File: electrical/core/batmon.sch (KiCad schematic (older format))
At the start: 25 parts

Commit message: Supply and Enable
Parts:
- gave numbers to parts that had none: 25
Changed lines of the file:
@@
 $Descr A4 11693 8268
 encoding utf-8
-Sheet 7 7
+Sheet 7 8
 Title ""
 Date ""
@@
 $EndDescr
 $Comp
-L rasbot:BQ76925 U?
+L rasbot:BQ76925 U5
 U 1 1 5D9FCD19
 P 5750 3650
-F 0 "U?" H 5750 4531 50  0000 C CNN
+F 0 "U5" H 5750 4531 50  0000 C CNN
 F 1 "BQ76925" H 5750 4440 50  0000 C CNN
 F 2 "Package_SO:TSSOP-20_4.4x6.5mm_P0.65mm" H 5650 3950 50  0001 C CNN
@@
 $EndComp
 $Comp
-L Device:R RIN?
+L Device:R RIN1
 U 1 1 5D9FCD1F
 P 3400 2700
-F 0 "RIN?" V 3193 2700 50  0000 C CNN
+F 0 "RIN1" V 3193 2700 50  0000 C CNN
 F 1 "47" V 3284 2700 50  0000 C CNN
 F 2 "Resistor_SMD:R_0805_2012Metric" V 3330 2700 50  0001 C CNN
@@
 $EndComp
 $Comp
-L Device:R RIN?
+L Device:R RIN2
 U 1 1 5D9FCD25
 P 3400 3200
-F 0 "RIN?" V 3193 3200 50  0000 C CNN
+F 0 "RIN2" V 3193 3200 50  0000 C CNN
 F 1 "47" V 3284 3200 50  0000 C CNN
 F 2 "Resistor_SMD:R_0805_2012Metric" V 3330 3200 50  0001 C CNN
@@
 $EndComp
 $Comp
-L Device:C CIN?
+L Device:C CIN2
 U 1 1 5D9FCD2B
 P 3800 3450
-F 0 "CIN?" H 3915 3496 50  0000 L CNN
+F 0 "CIN2" H 3915 3496 50  0000 L CNN
 F 1 "1u" H 3915 3405 50  0000 L CNN
 F 2 "Capacitor_SMD:C_0805_2012Metric" H 3838 3300 50  0001 C CNN
@@
 $EndComp
 $Comp
-L Device:R RIN?
+L Device:R RIN3
 U 1 1 5D9FCD31
 P 3400 3700
-F 0 "RIN?" V 3193 3700 50  0000 C CNN
+F 0 "RIN3" V 3193 3700 50  0000 C CNN
 F 1 "47" V 3284 3700 50  0000 C CNN
 F 2 "Resistor_SMD:R_0805_2012Metric" V 3330 3700 50  0001 C CNN
@@
 $EndComp
 $Comp
-L Device:C CIN?
+L Device:C CIN3
 U 1 1 5D9FCD37
 P 3800 3950
-F 0 "CIN?" H 3915 3996 50  0000 L CNN
+F 0 "CIN3" H 3915 3996 50  0000 L CNN
 F 1 "1u" H 3915 3905 50  0000 L CNN
 F 2 "Capacitor_SMD:C_0805_2012Metric" H 3838 3800 50  0001 C CNN
@@
 $EndComp
 $Comp
-L Device:R RIN?
+L Device:R RIN4
 U 1 1 5D9FCD3D
 P 3400 4200
-F 0 "RIN?" V 3193 4200 50  0000 C CNN
+F 0 "RIN4" V 3193 4200 50  0000 C CNN
 F 1 "47" V 3284 4200 50  0000 C CNN
 F 2 "Resistor_SMD:R_0805_2012Metric" V 3330 4200 50  0001 C CNN
@@
 $EndComp
 $Comp
-L Device:C CIN?
+L Device:C CIN1
 U 1 1 5D9FCD43
 P 3800 2950
-F 0 "CIN?" H 3915 2996 50  0000 L CNN
+F 0 "CIN1" H 3915 2996 50  0000 L CNN
 F 1 "1u" H 3915 2905 50  0000 L CNN
 F 2 "Capacitor_SMD:C_0805_2012Metric" H 3838 2800 50  0001 C CNN
@@
 	3550 4200 3800 4200
 $Comp
-L Connector:Conn_01x04_Male J?
+L Connector:Conn_01x04_Male J13
 U 1 1 5D9FCD55
 P 2050 3500
-F 0 "J?" H 1800 3300 50  0000 L CNN
+F 0 "J13" H 1800 3300 50  0000 L CNN
 F 1 "Conn_01x04" H 1800 3200 50  0000 L CNN
 F 2 "Connector_PinHeader_2.54mm:PinHeader_1x04_P2.54mm_Vertical" H 2050 3500 50  0001 C CNN
@@
 $EndComp
 $Comp
-L Device:C CIN?
+L Device:C CIN4
 U 1 1 5D9FCD5B
 P 3800 4450
-F 0 "CIN?" H 3915 4496 50  0000 L CNN
+F 0 "CIN4" H 3915 4496 50  0000 L CNN
 F 1 "1u" H 3915 4405 50  0000 L CNN
 F 2 "Capacitor_SMD:C_0805_2012Metric" H 3838 4300 50  0001 C CNN
@@
 	5750 4600 5750 4350
 $Comp
-L power:GND #PWR?
+L power:GND #PWR044
 U 1 1 5D9FCD71
 P 4600 4600
-F 0 "#PWR?" H 4600 4350 50  0001 C CNN
+F 0 "#PWR044" H 4600 4350 50  0001 C CNN
 F 1 "GND" H 4605 4427 50  0000 C CNN
 F 2 "" H 4600 4600 50  0001 C CNN
@@
 	4300 3700 3800 3700
 $Comp
-L power:GND #PWR?
+L power:GND #PWR045
 U 1 1 5D9FCD81
 P 4900 2450
-F 0 "#PWR?" H 4900 2200 50  0001 C CNN
+F 0 "#PWR045" H 4900 2200 50  0001 C CNN
 F 1 "GND" H 4905 2277 50  0000 C CNN
 F 2 "" H 4900 2450 50  0001 C CNN
@@
 	4650 2000 4900 2000
 $Comp
-L Device:C CBAT?
+L Device:C CBAT1
 U 1 1 5D9FCD8A
 P 4900 2200
-F 0 "CBAT?" H 5015 2246 50  0000 L CNN
+F 0 "CBAT1" H 5015 2246 50  0000 L CNN
 F 1 "10u" H 5015 2155 50  0000 L CNN
 F 2 "Capacitor_SMD:C_0805_2012Metric" H 4938 2050 50  0001 C CNN
@@
 $EndComp
 $Comp
-L Device:C COUT?
+L Device:C COUT2
 U 1 1 5D9FCD90
 P 5450 5050
-F 0 "COUT?" H 5565 5096 50  0000 L CNN
+F 0 "COUT2" H 5565 5096 50  0000 L CNN
 F 1 "1u" H 5565 5005 50  0000 L CNN
 F 2 "Capacitor_SMD:C_0805_2012Metric" H 5488 4900 50  0001 C CNN
@@
 $EndComp
 $Comp
-L Device:C COUT?
+L Device:C COUT1
 U 1 1 5D9FCD96
 P 4550 5050
-F 0 "COUT?" H 4665 5096 50  0000 L CNN
+F 0 "COUT1" H 4665 5096 50  0000 L CNN
 F 1 "1u" H 4665 5005 50  0000 L CNN
 F 2 "Capacitor_SMD:C_0805_2012Metric" H 4588 4900 50  0001 C CNN
@@
 Connection ~ 4550 4900
 $Comp
-L Device:C CREF?
+L Device:C CREF1
 U 1 1 5D9FCDA7
 P 8750 2850
-F 0 "CREF?" H 8865 2896 50  0000 L CNN
+F 0 "CREF1" H 8865 2896 50  0000 L CNN
 F 1 "10u" H 8865 2805 50  0000 L CNN
 F 2 "Capacitor_SMD:C_0805_2012Metric" H 8788 2700 50  0001 C CNN
@@
 $EndComp
 $Comp
-L power:GND #PWR?
+L power:GND #PWR048
 U 1 1 5D9FCDAD
 P 8000 3500
-F 0 "#PWR?" H 8000 3250 50  0001 C CNN
+F 0 "#PWR048" H 8000 3250 50  0001 C CNN
 F 1 "GND" H 8005 3327 50  0000 C CNN
 F 2 "" H 8000 3500 50  0001 C CNN
@@
 $EndComp
 $Comp
-L power:GND #PWR?
+L power:GND #PWR046
 U 1 1 5D9FCDB3
 P 5000 5350
-F 0 "#PWR?" H 5000 5100 50  0001 C CNN
+F 0 "#PWR046" H 5000 5100 50  0001 C CNN
 F 1 "GND" H 5005 5177 50  0000 C CNN
 F 2 "" H 5000 5350 50  0001 C CNN
@@
 Battery_OvercurrentAlert
 $Comp
-L Device:C CSENSE?
+L Device:C CSENSE1
 U 1 1 5D9FCDC2
 P 7850 4850
-F 0 "CSENSE?" V 8100 4800 50  0000 L CNN
+F 0 "CSENSE1" V 8100 4800 50  0000 L CNN
 F 1 "0.1u" V 8000 4800 50  0000 L CNN
 F 2 "Capacitor_SMD:C_0805_2012Metric" H 7888 4700 50  0001 C CNN
@@
 $EndComp
 $Comp
-L Device:R RSENSEN?
+L Device:R RSENSEN1
 U 1 1 5D9FCDC8
 P 7250 5200
-F 0 "RSENSEN?" H 7000 5300 50  0000 C CNN
+F 0 "RSENSEN1" H 7000 5300 50  0000 C CNN
 F 1 "1k" H 7134 5200 50  0000 C CNN
 F 2 "Resistor_SMD:R_0805_2012Metric" V 7180 5200 50  0001 C CNN
@@
 $EndComp
 $Comp
-L Device:R RSENSEP?
+L Device:R RSENSEP1
 U 1 1 5D9FCDCE
 P 8550 5200
-F 0 "RSENSEP?" H 8300 5300 50  0000 C CNN
+F 0 "RSENSEP1" H 8300 5300 50  0000 C CNN
 F 1 "1k" H 8434 5200 50  0000 C CNN
 F 2 "Resistor_SMD:R_0805_2012Metric" V 8480 5200 50  0001 C CNN
@@
 	8550 4850 8550 5050
 $Comp
-L power:-BATT #PWR?
+L power:-BATT #PWR049
 U 1 1 5D9FCDD8
 P 8550 5900
-F 0 "#PWR?" H 8550 5750 50  0001 C CNN
+F 0 "#PWR049" H 8550 5750 50  0001 C CNN
 F 1 "-BATT" H 8565 6073 50  0000 C CNN
 F 2 "" H 8550 5900 50  0001 C CNN
@@
 Battery_PackCurrent
 $Comp
-L power:+BATT #PWR?
+L power:+BATT #PWR043
 U 1 1 5D9FCDF2
 P 3800 1550
-F 0 "#PWR?" H 3800 1400 50  0001 C CNN
+F 0 "#PWR043" H 3800 1400 50  0001 C CNN
 F 1 "+BATT" H 3815 1723 50  0000 C CNN
 F 2 "" H 3800 1550 50  0001 C CNN
@@
 Connection ~ 4900 2000
 $Comp
-L Device:R RBAT?
+L Device:R RBAT1
 U 1 1 5D9FCDFB
 P 4500 2000
-F 0 "RBAT?" V 4293 2000 50  0000 C CNN
+F 0 "RBAT1" V 4293 2000 50  0000 C CNN
 F 1 "100" V 4384 2000 50  0000 C CNN
 F 2 "Resistor_SMD:R_0805_2012Metric" V 4430 2000 50  0001 C CNN
@@
 Connection ~ 5750 2950
 $Comp
-L Diode:BZT52Bxx D?
+L Diode:BZT52Bxx D5
 U 1 1 5D9FCE05
 P 5600 2250
-F 0 "D?" V 5600 2466 50  0000 C CNN
+F 0 "D5" V 5600 2466 50  0000 C CNN
 F 1 "BZT52C30" V 5700 2450 50  0000 C CNN
 F 2 "Diode_SMD:D_SOD-123" H 5600 2075 50  0001 C CNN
@@
 	4900 2400 4900 2450
 $Comp
-L Diode:MBR0540 D?
+L Diode:MBR0540 D4
 U 1 1 5D9FCE13
 P 4100 2000
-F 0 "D?" H 4100 2216 50  0000 C CNN
+F 0 "D4" H 4100 2216 50  0000 C CNN
 F 1 "MBR0540" H 4100 2125 50  0000 C CNN
 F 2 "Diode_SMD:D_SOD-123" H 4100 1825 50  0001 C CNN
@@
 LDO_3.3V
 $Comp
-L power:GND #PWR?
+L power:GND #PWR047
 U 1 1 5D9FCE1B
 P 7250 5900
-F 0 "#PWR?" H 7250 5650 50  0001 C CNN
+F 0 "#PWR047" H 7250 5650 50  0001 C CNN
 F 1 "GND" H 7255 5727 50  0000 C CNN
 F 2 "" H 7250 5900 50  0001 C CNN
@@
 	7250 5750 7250 5900
 $Comp
-L Device:R RTH?
+L Device:R RTH1
 U 1 1 5D9FCE2B
 P 6900 3100
-F 0 "RTH?" V 6693 3100 50  0000 C CNN
+F 0 "RTH1" V 6693 3100 50  0000 C CNN
 F 1 "10k" V 6784 3100 50  0000 C CNN
 F 2 "Resistor_SMD:R_0805_2012Metric" V 6830 3100 50  0001 C CNN
@@
 	6500 3100 6750 3100
 $Comp
-L Device:C CTH?
+L Device:C CTH1
 U 1 1 5D9FCE33
 P 7300 3350
-F 0 "CTH?" H 7415 3396 50  0000 L CNN
+F 0 "CTH1" H 7415 3396 50  0000 L CNN
 F 1 "1u" H 7415 3305 50  0000 L CNN
 F 2 "Capacitor_SMD:C_0805_2012Metric" H 7338 3200 50  0001 C CNN
@@
 	7300 3100 7300 3200
 $Comp
-L Device:Thermistor_NTC TH?
+L Device:Thermistor_NTC TH1
 U 1 1 5D9FCE3A
 P 8000 3350
-F 0 "TH?" H 8098 3396 50  0000 L CNN
+F 0 "TH1" H 8098 3396 50  0000 L CNN
 F 1 "NCP21XV103J03RA" H 8098 3305 50  0000 L CNN
 F 2 "Resistor_SMD:R_0805_2012Metric" H 8000 3400 50  0001 C CNN
@@
 Connection ~ 8000 3100
 $Comp
-L Device:R R?
+L Device:R R19
 U 1 1 5D9FCE51
 P 7850 5400
-F 0 "R?" V 7643 5400 50  0000 C CNN
+F 0 "R19" V 7643 5400 50  0000 C CNN
 F 1 "R" V 7734 5400 50  0000 C CNN
 F 2 "" V 7780 5400 50  0001 C CNN
@@
 	7250 5400 7700 5400
 $Comp
-L Device:R R?
+L Device:R R20
 U 1 1 5D9FCE5A
 P 7850 5750
-F 0 "R?" V 7643 5750 50  0000 C CNN
+F 0 "R20" V 7643 5750 50  0000 C CNN
 F 1 "R" V 7734 5750 50  0000 C CNN
 F 2 "" V 7780 5750 50  0001 C CNN

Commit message: redid NTC connection to the BMS and changed current sense resistors
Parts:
- removed CREF1: 10u, Capacitor_SMD:C_0805_2012Metric, symbol Device:C
- removed TH1: NCP21XV103J03RA, Resistor_SMD:R_0805_2012Metric, symbol Device:Thermistor_NTC
- added J14: Conn_01x02_Male, Connector_PinHeader_2.54mm:PinHeader_1x02_P2.54mm_Vertical, symbol Connector:Conn_01x02_Male
- R19, R20: value R -> 2m; footprint (none) -> Resistor_SMD:R_2512_6332Metric; Notes WSL-2512 .002 1% -> Current Sense resistor 2m 1% 1W(min)
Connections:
- net labels removed: Battery_Temp, Battery_VREF, LDO_3.3V
- wire segments 97 -> 93
- no-connect marks 0 -> 2
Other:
- note added: "ADC Note: Vref is not connected to the MCU, minor errors may occur\n"
- note added: "LDO 3.3V\n"
- note added: "NTC Header"
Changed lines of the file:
@@
 EESchema Schematic File Version 4
 LIBS:core-cache
-EELAYER 30 0
+EELAYER 26 0
 EELAYER END
 $Descr A4 11693 8268
@@
 Connection ~ 4550 4900
 $Comp
-L Device:C CREF1
-U 1 1 5D9FCDA7
-P 8750 2850
-F 0 "CREF1" H 8865 2896 50  0000 L CNN
-F 1 "10u" H 8865 2805 50  0000 L CNN
-F 2 "Capacitor_SMD:C_0805_2012Metric" H 8788 2700 50  0001 C CNN
-F 3 "~" H 8750 2850 50  0001 C CNN
-	1    8750 2850
-	1    0    0    -1
-$EndComp
-$Comp
-L power:GND #PWR048
-U 1 1 5D9FCDAD
-P 8000 3500
-F 0 "#PWR048" H 8000 3250 50  0001 C CNN
-F 1 "GND" H 8005 3327 50  0000 C CNN
-F 2 "" H 8000 3500 50  0001 C CNN
-F 3 "" H 8000 3500 50  0001 C CNN
-	1    8000 3500
-	1    0    0    -1
-$EndComp
-$Comp
 L power:GND #PWR046
 U 1 1 5D9FCDB3
@@
 	5450 5200 5000 5200
 Connection ~ 5000 5200
-Text HLabel 9050 2700 2    50   Output ~ 0
-Battery_VREF
 Text HLabel 5700 4900 2    50   Output ~ 0
 Battery_CellVoltage
@@
 Wire Wire Line
 	3950 2000 3800 2000
-Text Label 6150 3550 0    50   ~ 0
-LDO_3.3V
 $Comp
 L power:GND #PWR047
@@
 	7250 5750 7250 5900
 $Comp
+L Device:R R19
+U 1 1 5D9FCE51
+P 7850 5400
+F 0 "R19" V 7643 5400 50  0000 C CNN
+F 1 "2m" V 7734 5400 50  0000 C CNN
+F 2 "Resistor_SMD:R_2512_6332Metric" V 7780 5400 50  0001 C CNN
+F 3 "https://industrial.panasonic.com/cdbs/www-data/pdf/RDN0000/AOA0000C90.pdf" H 7850 5400 50  0001 C CNN
+F 4 "Current Sense resistor 2m 1% 1W(min)" V 7850 5400 50  0001 C CNN "Notes"
+	1    7850 5400
+	0    1    1    0
+$EndComp
+Wire Wire Line
+	8000 5400 8550 5400
+Wire Wire Line
+	7250 5400 7700 5400
+$Comp
+L Device:R R20
+U 1 1 5D9FCE5A
+P 7850 5750
+F 0 "R20" V 7643 5750 50  0000 C CNN
+F 1 "2m" V 7734 5750 50  0000 C CNN
+F 2 "Resistor_SMD:R_2512_6332Metric" V 7780 5750 50  0001 C CNN
+F 3 "https://industrial.panasonic.com/cdbs/www-data/pdf/RDN0000/AOA0000C90.pdf" H 7850 5750 50  0001 C CNN
+F 4 "Current Sense resistor 2m 1% 1W(min)" V 7850 5750 50  0001 C CNN "Notes"
+	1    7850 5750
+	0    1    1    0
+$EndComp
+Wire Wire Line
+	8000 5750 8550 5750
+Wire Wire Line
+	7250 5750 7700 5750
+Wire Wire Line
+	6500 3350 6500 3100
+Wire Wire Line
+	6150 3350 6500 3350
+Wire Wire Line
+	7300 3100 7300 3200
+$Comp
+L Device:C CTH1
+U 1 1 5D9FCE33
+P 7300 3350
+F 0 "CTH1" H 7415 3396 50  0000 L CNN
+F 1 "1u" H 7415 3305 50  0000 L CNN
+F 2 "Capacitor_SMD:C_0805_2012Metric" H 7338 3200 50  0001 C CNN
+F 3 "~" H 7300 3350 50  0001 C CNN
+	1    7300 3350
+	1    0    0    -1
+$EndComp
+Wire Wire Line
+	6500 3100 6750 3100
+Wire Wire Line
+	7050 3100 7300 3100
+$Comp
 L Device:R RTH1
 U 1 1 5D9FCE2B
@@
 $EndComp
 Wire Wire Line
-	7050 3100 7300 3100
-Wire Wire Line
-	6500 3100 6750 3100
-$Comp
-L Device:C CTH1
-U 1 1 5D9FCE33
-P 7300 3350
-F 0 "CTH1" H 7415 3396 50  0000 L CNN
-F 1 "1u" H 7415 3305 50  0000 L CNN
-F 2 "Capacitor_SMD:C_0805_2012Metric" H 7338 3200 50  0001 C CNN
-F 3 "~" H 7300 3350 50  0001 C CNN
-	1    7300 3350
-	1    0    0    -1
-$EndComp
-Wire Wire Line
-	7300 3100 7300 3200
-$Comp
-L Device:Thermistor_NTC TH1
-U 1 1 5D9FCE3A
-P 8000 3350
-F 0 "TH1" H 8098 3396 50  0000 L CNN
-F 1 "NCP21XV103J03RA" H 8098 3305 50  0000 L CNN
-F 2 "Resistor_SMD:R_0805_2012Metric" H 8000 3400 50  0001 C CNN
-F 3 "https://www.murata.com/~/media/webrenewal/support/library/catalog/products/thermistor/ntc/r44e.ashx?la=en-us" H 8000 3400 50  0001 C CNN
-	1    8000 3350
-	1    0    0    -1
-$EndComp
-Wire Wire Line
-	8000 3200 8000 3100
-Wire Wire Line
-	8000 3100 7300 3100
+	7300 3500 8000 3500
+$Comp
+L power:GND #PWR048
+U 1 1 5D9FCDAD
+P 8000 3500
+F 0 "#PWR048" H 8000 3250 50  0001 C CNN
+F 1 "GND" H 8005 3327 50  0000 C CNN
+F 2 "" H 8000 3500 50  0001 C CNN
+F 3 "" H 8000 3500 50  0001 C CNN
+	1    8000 3500
+	1    0    0    -1
+$EndComp
+NoConn ~ 6150 3250
+NoConn ~ 6150 3550
+$Comp
+L Connector:Conn_01x02_Male J14
+U 1 1 5D5860BC
+P 8950 3100
+F 0 "J14" H 8923 3073 50  0000 R CNN
+F 1 "Conn_01x02_Male" H 8923 2982 50  0000 R CNN
+F 2 "Connector_PinHeader_2.54mm:PinHeader_1x02_P2.54mm_Vertical" H 8950 3100 50  0001 C CNN
+F 3 "~" H 8950 3100 50  0001 C CNN
+	1    8950 3100
+	-1   0    0    -1
+$EndComp
+Wire Wire Line
+	8200 3200 8200 3500
+Wire Wire Line
+	8750 3200 8200 3200
+Wire Wire Line
+	7300 3100 8750 3100
 Connection ~ 7300 3100
 Wire Wire Line
-	8750 3000 8750 3500
-Wire Wire Line
-	8750 3500 8000 3500
+	8000 3500 8200 3500
 Connection ~ 8000 3500
-Wire Wire Line
-	7300 3500 8000 3500
-Wire Wire Line
-	6150 3250 6150 2700
-Wire Wire Line
-	9050 2700 8750 2700
-Connection ~ 8750 2700
-Wire Wire Line
-	8750 2700 6150 2700
-Wire Wire Line
-	6150 3350 6500 3350
-Wire Wire Line
-	6500 3350 6500 3100
-Text HLabel 8100 3100 2    50   Output ~ 0
-Battery_Temp
-Wire Wire Line
-	8100 3100 8000 3100
-Connection ~ 8000 3100
-$Comp
-L Device:R R19
-U 1 1 5D9FCE51
-P 7850 5400
-F 0 "R19" V 7643 5400 50  0000 C CNN
-F 1 "R" V 7734 5400 50  0000 C CNN
-F 2 "" V 7780 5400 50  0001 C CNN
-F 3 "~" H 7850 5400 50  0001 C CNN
-F 4 "WSL-2512 .002 1%" V 7850 5400 50  0001 C CNN "Notes"
-	1    7850 5400
-	0    1    1    0
-$EndComp
-Wire Wire Line
-	8000 5400 8550 5400
-Wire Wire Line
-	7250 5400 7700 5400
-$Comp
-L Device:R R20
-U 1 1 5D9FCE5A
-P 7850 5750
-F 0 "R20" V 7643 5750 50  0000 C CNN
-F 1 "R" V 7734 5750 50  0000 C CNN
-F 2 "" V 7780 5750 50  0001 C CNN
-F 3 "~" H 7850 5750 50  0001 C CNN
-F 4 "WSL-2512 .002 1%" V 7850 5750 50  0001 C CNN "Notes"
-	1    7850 5750
-	0    1    1    0
-$EndComp
-Wire Wire Line
-	8000 5750 8550 5750
-Wire Wire Line
-	7250 5750 7700 5750
+Text Notes 9000 3350 0    50   ~ 0
+NTC Header
+Text Notes 6150 3550 0    50   ~ 0
+LDO 3.3V\n
+Text Notes 6300 2700 0    50   ~ 0
+ADC Note: Vref is not connected to the MCU, minor errors may occur\n
 $EndSCHEMATC

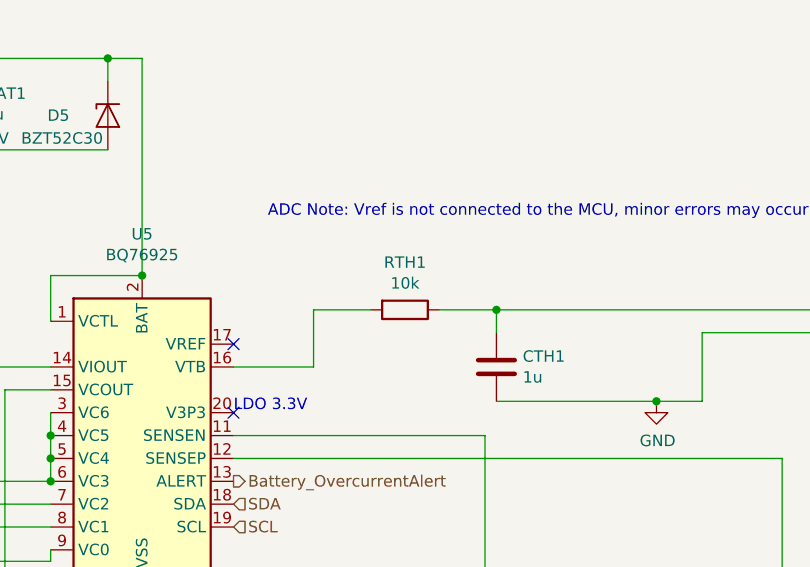
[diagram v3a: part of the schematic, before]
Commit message: NTC resistance changed
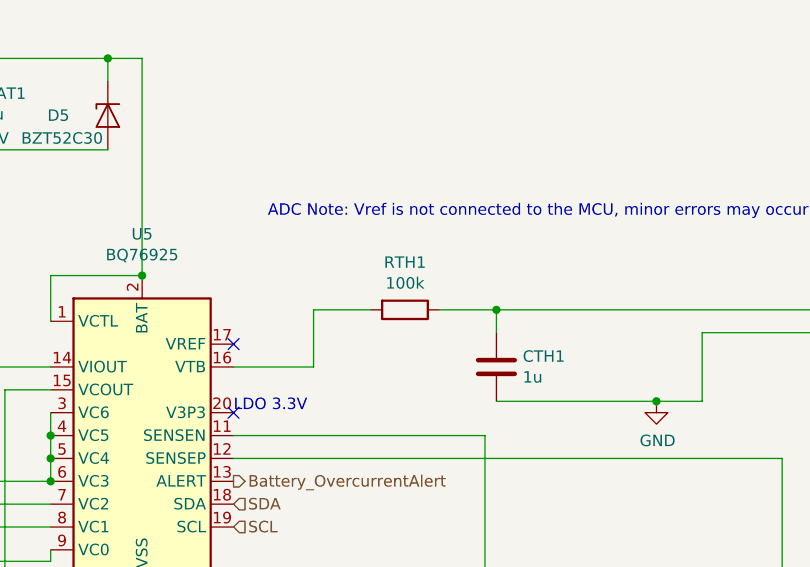
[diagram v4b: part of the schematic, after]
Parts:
- RTH1: value 10k -> 100k
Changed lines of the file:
@@
 P 6900 3100
 F 0 "RTH1" V 6693 3100 50  0000 C CNN
-F 1 "10k" V 6784 3100 50  0000 C CNN
+F 1 "100k" V 6784 3100 50  0000 C CNN
 F 2 "Resistor_SMD:R_0805_2012Metric" V 6830 3100 50  0001 C CNN
 F 3 "~" H 6900 3100 50  0001 C CNN
